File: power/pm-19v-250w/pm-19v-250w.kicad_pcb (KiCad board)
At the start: 4 copper layers, 58.4 x 22.9 mm, 57 parts, among them J1 Screw pads S1-S4, J2 Aux pads 2x3, Q1 BSC070N10NS5, Q2 BSC070N10NS5, Q3 BSC070N10NS5, Q4 BSC070N10NS5, U1 LTC7810, U2 MCP65R46-1.21, U3 MCP65R46-1.21

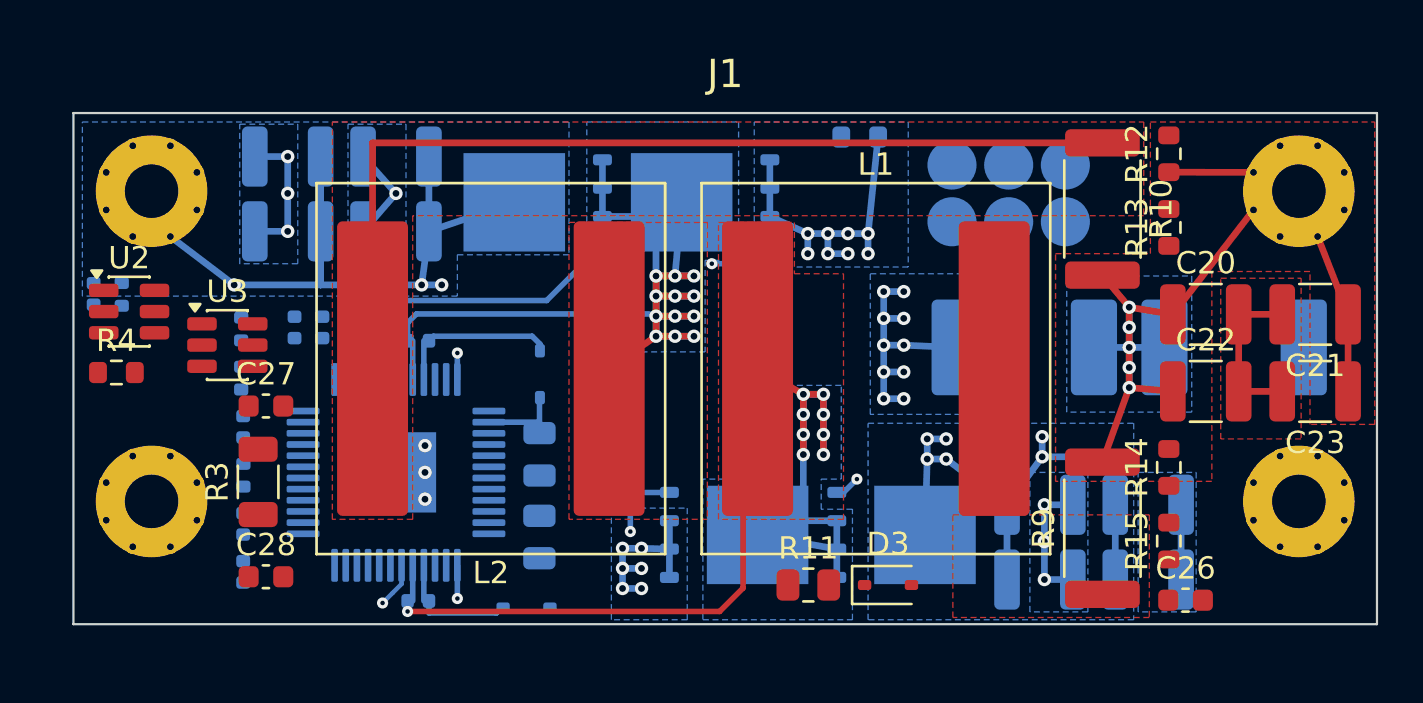
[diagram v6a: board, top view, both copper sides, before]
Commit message: pm-19v-250w: supervision block grouped at the input end (dividers and VAUX caps to 0402), RUN/OVLO divider on B at the input end, R16 by J2; hand drive routes kept (group 'hand', krt keep_groups); KRT routed the rest: 14 opens left (VOUT, OVLO, ITH1, INTVCC, DRVCC/NDRV, U2-, U3+, GND taps), 0 clearance errors
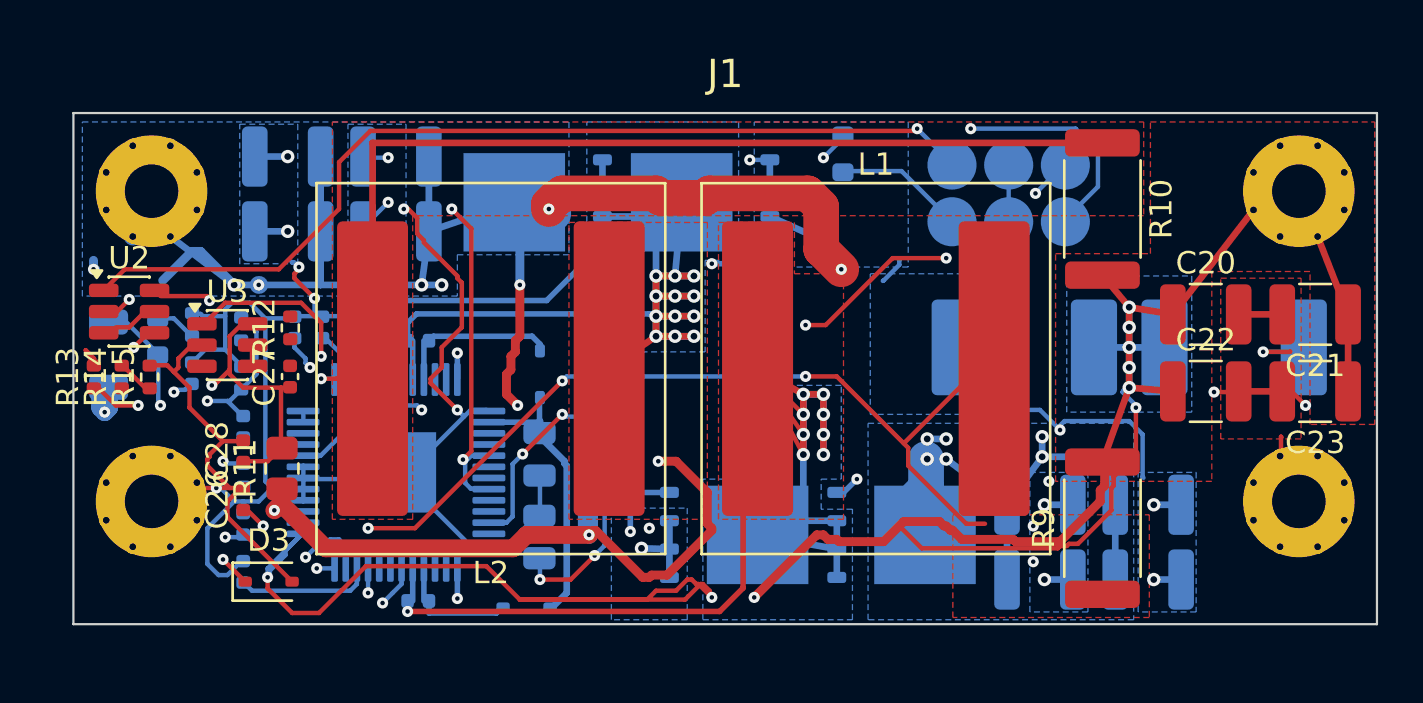
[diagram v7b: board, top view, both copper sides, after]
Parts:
- C26, C27, C28: footprint Capacitor_SMD:C_0603_1608Metric -> Capacitor_SMD:C_0402_1005Metric
- R12, R13, R14, R15: footprint Resistor_SMD:R_0603_1608Metric -> Resistor_SMD:R_0402_1005Metric
- R3, R4: moved to B.Cu
- moved R13 48.6 mm to (100.9, 111.8)
- moved R14 47.1 mm to (102.2, 111.8)
- moved R15 46.2 mm to (103.4, 111.8)
- moved C26 42.5 mm to (107.6, 117.3), turned to 90 degrees
- moved R12 40.1 mm to (109.7, 109.6)
- moved D3 27.8 mm to (108.7, 121.0)
- moved R11 24.2 mm to (109.3, 115.9), turned to 90 degrees
- moved R3 8.80 mm to (101.6, 110.8)
- moved C28 5.71 mm to (107.6, 115.2), turned to 90 degrees
- moved C15 5.65 mm to (105.3, 111.7)
- moved R5 3.43 mm to (105.3, 109.5)
- moved R4 2.45 mm to (103.8, 110.0), turned to 90 degrees
- moved C27 1.71 mm to (109.7, 111.8), turned to 90 degrees
- moved R16 1.06 mm to (134.5, 101.8), turned to 90 degrees
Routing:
- net /VIN: track 69.9 -> 198.1 mm, vias 9 -> 19
- net GND: track 62.1 -> 146.5 mm, vias 34 -> 23
- net /RUN: track 0.00 -> 75.1 mm, vias 0 -> 4
- net /VOUT: track 50.6 -> 124.9 mm, vias 5 -> 9
- net /SNS1P: track 0.00 -> 45.3 mm, vias 0 -> 6
- net /PGOOD: track 0.00 -> 44.7 mm, vias 0 -> 4
- net /OV_KILL: track 0.00 -> 42.7 mm, vias 0 -> 1
- net Net-(U1-VFB1): track 0.00 -> 32.5 mm, vias 0 -> 2
- net /VAUX: track 0.00 -> 29.0 mm, vias 0 -> 4
- net Net-(U1-TRACK/SS1): track 0.00 -> 28.5 mm, vias 0 -> 2
- net /VIN_IC: track 0.00 -> 18.1 mm, vias 0 -> 4
- net Net-(U1-ITH2): track 0.00 -> 12.1 mm, vias 0 -> 2
- net /SW1: track 46.5 -> 57.5 mm
- net /DRVCC: track 3.37 -> 12.7 mm
- net Net-(U2--): track 0.00 -> 6.30 mm, vias 0 -> 2
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- added copper zone on In2.Cu, net GND

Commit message: pm-19v-250w: R10 beside L2 pad 2 (phase 2 strip drop out of the sense loop, no VIN trace on F), input end hand-routed (tools/route_input.py: Kelvin SENSE1/2, compensation on F, RUN/NDRV under U1 on In1), comparators moved to the output end, KRT for the rest, route_post.py restores ITH1/C13; 0 opens, 0 clearance errors
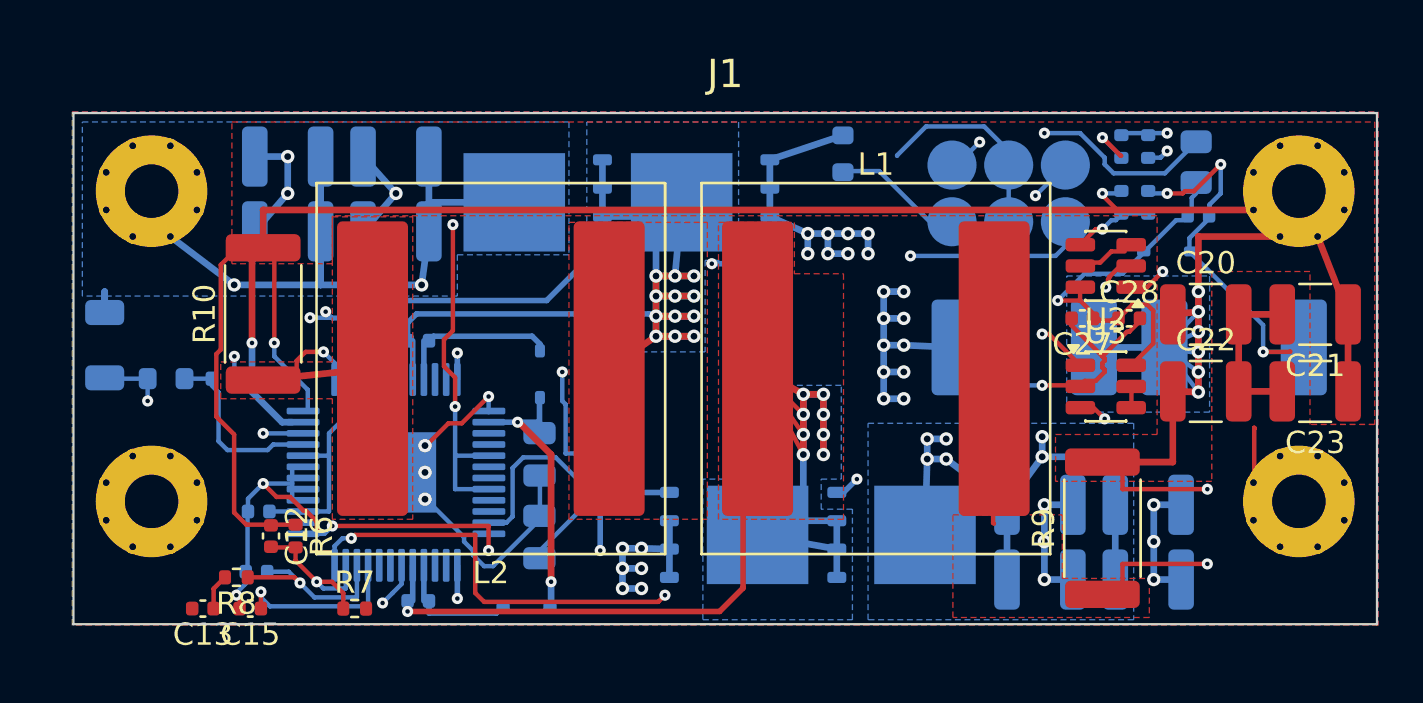
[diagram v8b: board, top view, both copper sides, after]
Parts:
- C12, C13, C15, R6, R7, R8: moved to F.Cu
- C26, D3, R11, R12, R13, R14, R15: moved to B.Cu
- moved R13 47.9 mm to (148.2, 104.0)
- moved R14 46.0 mm to (146.9, 101.5)
- moved R15 45.9 mm to (148.2, 101.5), turned to -90 degrees
- moved C26 44.6 mm to (150.4, 104.6), turned to 0 degrees
- moved U2 43.8 mm to (146.2, 106.8), turned to 180 degrees
- moved R11 43.2 mm to (150.3, 102.2), turned to -90 degrees
- moved D3 42.9 mm to (149.0, 106.2)
- moved C28 40.1 mm to (147.3, 109.2), turned to 0 degrees
- moved U3 39.4 mm to (146.2, 112.2)
- moved R10 37.9 mm to (108.5, 109.0), turned to 90 degrees
- moved R12 37.7 mm to (146.9, 104.0), turned to -90 degrees
- moved C27 35.6 mm to (145.2, 109.2), turned to 180 degrees
- moved R7 11.5 mm to (112.6, 122.2), turned to 0 degrees
- moved C15 10.9 mm to (107.9, 122.2), turned to 180 degrees
- moved R6 9.59 mm to (110.0, 119.0), turned to -90 degrees
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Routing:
- net /VIN: track 198.1 -> 97.5 mm, vias 19 -> 10
- net /VOUT: track 124.9 -> 186.7 mm, vias 9 -> 13
- net /SNS2P: track 44.2 -> 7.70 mm
- net /PGOOD: track 44.7 -> 10.4 mm, vias 4 -> 2
- net /OV_KILL: track 42.7 -> 13.7 mm, vias 1 -> 2
- net Net-(U1-VFB1): track 32.5 -> 6.95 mm, vias 2 -> 1
- net Net-(U1-TRACK/SS1): track 28.5 -> 7.17 mm, vias 2 -> 1
- net Net-(U3-+): track 1.69 -> 17.1 mm, vias 0 -> 2
- net /DRVCC: track 12.7 -> 26.4 mm, vias 0 -> 3
- net /RUN: track 75.1 -> 61.5 mm
- net /VAUX: track 29.0 -> 16.3 mm, vias 4 -> 1
- net Net-(U1-ITH2): track 12.1 -> 1.23 mm, vias 2 -> 0
- net /SNS1P: track 45.3 -> 54.8 mm, vias 6 -> 3
- net GND: track 146.5 -> 139.2 mm, vias 23 -> 48
- net /OVLO: track 1.88 -> 7.41 mm
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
